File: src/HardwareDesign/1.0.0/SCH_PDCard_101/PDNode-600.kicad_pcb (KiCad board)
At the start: 6 copper layers, 53.9 x 35.5 mm, 132 parts, among them IC1 TPS552882QRPMRQ1, IC2 MCP22350T-2I/Q8X, IC3 INA219BIDCNT, IC4 SN74LVC1G97QDCKRQ1, IC5 SN74LVC1G97QDCKRQ1, IC6 TPS74801DRCT, IC7 SN74LVC1G97QDCKRQ1, J1 USB_C_Receptacle_PowerOnly_6P, J2 PCIE EDGE CONNECTOR, T1 BSZ065N06, T2 BSZ065N06, T3 DMP3013SFV, T4 DMP3013SFV, T5 DMP3013SFV, U1 24AA02E-OT

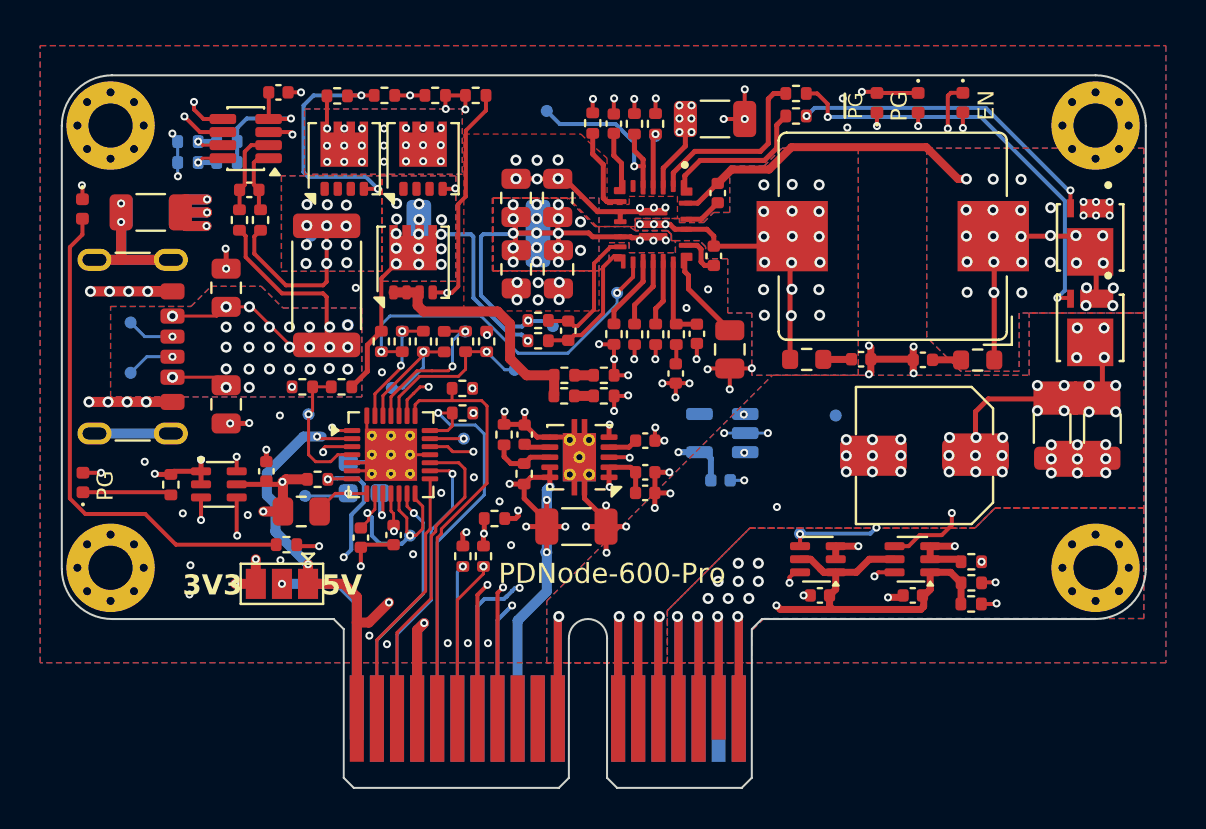
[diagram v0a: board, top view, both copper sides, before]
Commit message: update component lib
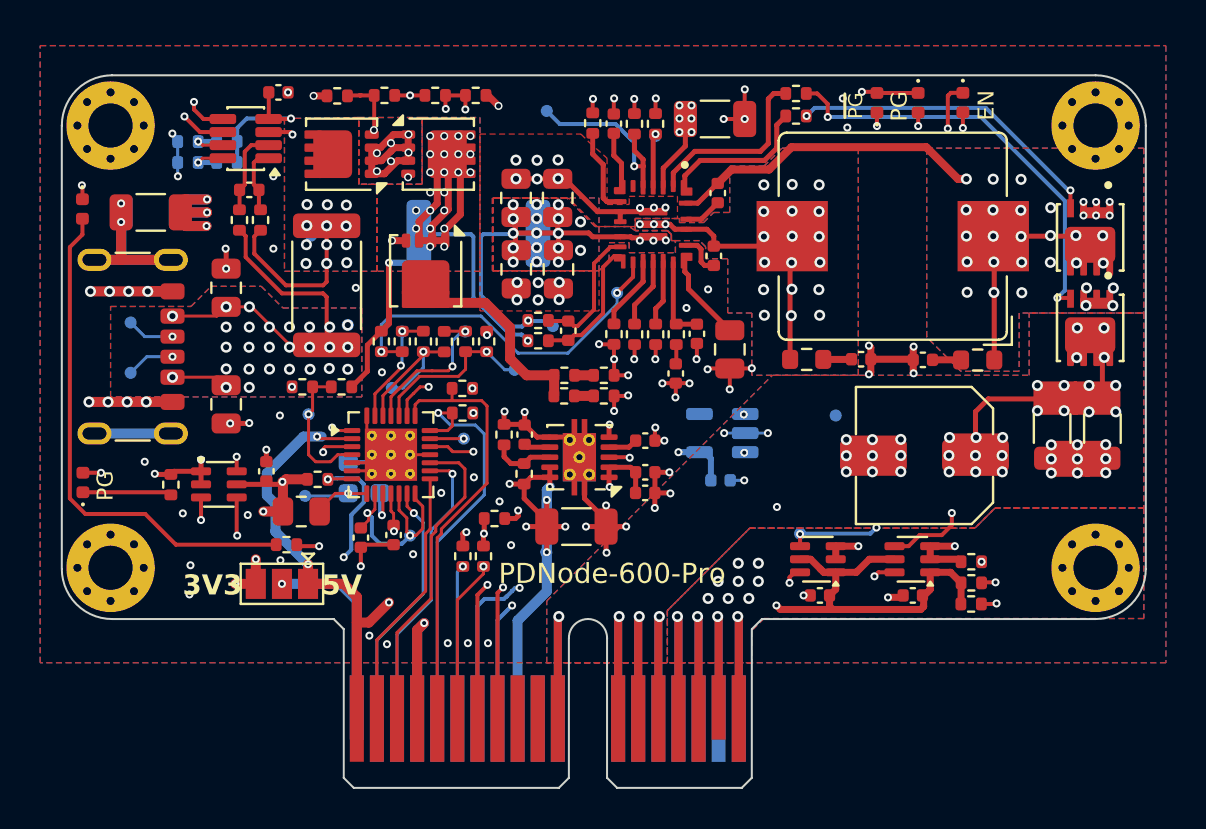
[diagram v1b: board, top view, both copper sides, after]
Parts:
- moved T3 0.79 mm to (162.3, 66.9), turned to 0 degrees
- moved T5 0.76 mm to (161.7, 72.7), turned to -90 degrees
- moved T4 0.26 mm to (157.5, 66.9), turned to 180 degrees
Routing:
- net /Block Diagram/USB-PD Source Controller/V_SOURCE: track 15.4 -> 33.7 mm, vias 15 -> 24
- net /Block Diagram/USB-PD Source Controller/T3T4DS: track 1.66 -> 15.3 mm, vias 21 -> 7
- net Net-(T3-G): track 17.1 -> 9.14 mm, vias 3 -> 2
- net /Block Diagram/Adjustable 5A Buck Converter/SW1: track 29.9 -> 27.2 mm
- net Net-(R17-Pad1): track 14.7 -> 12.4 mm
- net /Block Diagram/USB-PD Source Controller/DISCHARGE: track 25.1 -> 25.9 mm, vias 2 -> 3
- net GND: track 176.0 -> 175.4 mm, vias 146 -> 148
